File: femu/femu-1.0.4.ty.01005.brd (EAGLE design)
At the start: 24.1 x 15.8 mm, 56 parts, among them IC1 ESP32-QFN_5X5

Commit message: Adjusting RF matching components to improve waveguide and ground plane
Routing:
- net GND: track 93.7 -> 94.2 mm
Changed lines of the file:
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@@
 <via x="14.8788" y="10.7696" extent="15-16" drill="0.1016" diameter="0.3048"/>
 <via x="14.7828" y="10.318" extent="15-16" drill="0.1016" diameter="0.3048"/>
+<wire x1="12.3774" y1="10.3378" x2="12.9484" y2="10.3378" width="0.1524" layer="16"/>
 </signal>
 <signal name="XOUT">

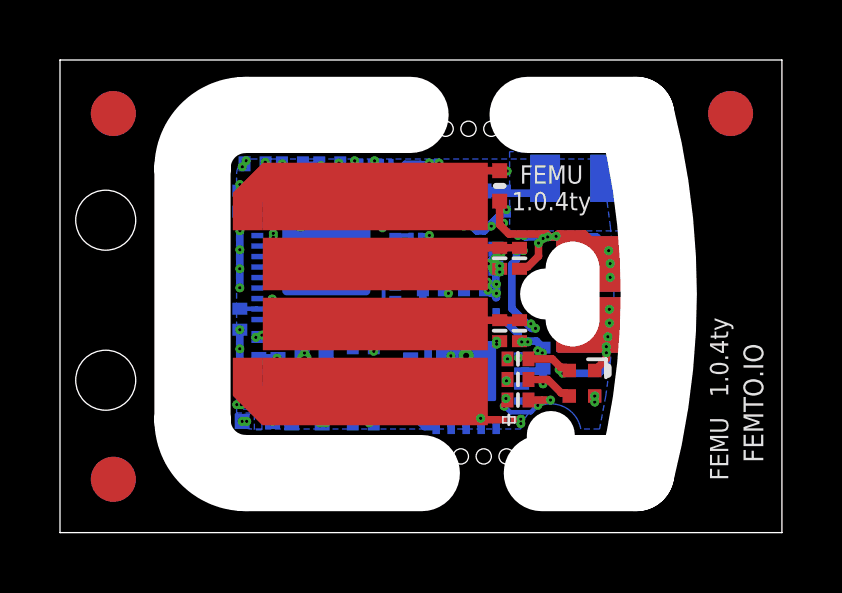
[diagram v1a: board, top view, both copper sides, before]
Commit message: Adjusting ty antenna variant with 01005 parts
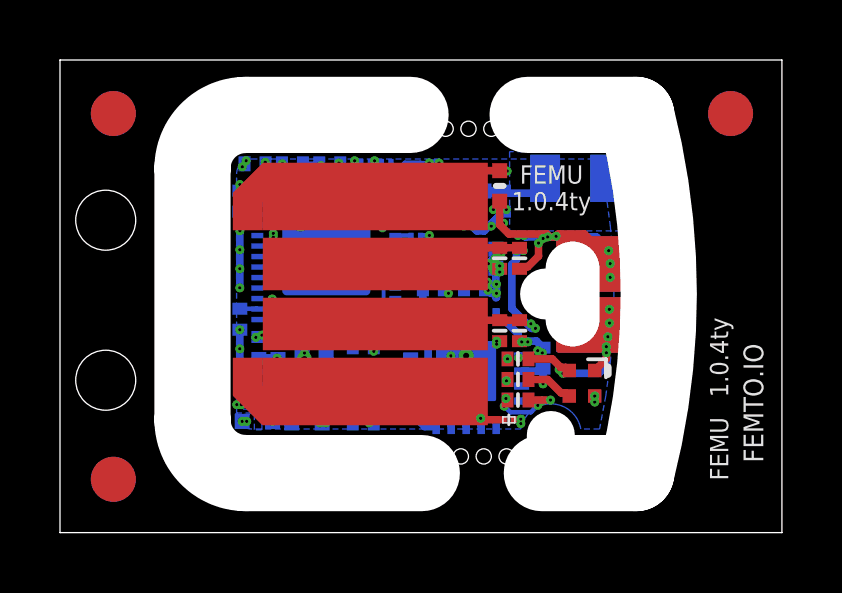
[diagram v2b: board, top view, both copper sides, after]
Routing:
- net GND: vias 120 -> 124
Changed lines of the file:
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@@
 <via x="14.7828" y="10.318" extent="15-16" drill="0.1016" diameter="0.3048"/>
 <wire x1="12.3774" y1="10.3378" x2="12.9484" y2="10.3378" width="0.1524" layer="16"/>
+<via x="13.1516" y="10.7696" extent="15-16" drill="0.1016" diameter="0.3048"/>
+<via x="13.5834" y="10.7696" extent="15-16" drill="0.1016" diameter="0.3048"/>
+<via x="14.0152" y="10.7696" extent="15-16" drill="0.1016" diameter="0.3048"/>
+<via x="14.447" y="10.7696" extent="15-16" drill="0.1016" diameter="0.3048"/>
 </signal>
 <signal name="XOUT">
